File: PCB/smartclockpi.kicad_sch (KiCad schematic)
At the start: 17 parts, among them J1 Raspberry_Pi_2_3, J2 DS3231 RTC module, J3 ILI9488 SPI TFT touchscreen, J4 PCM5102A DAC (with headphone 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, U1 BME280, U2 MCP3008

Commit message: finallise pcb. spent toooo much time on this...
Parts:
- removed R10, R11: 4.7kΩ, Resistor_THT:R_Axial_DIN0204_L3.6mm_D1.6mm_P5.08mm_Vertical, symbol Device:R
- removed U1: BME280, Connector_PinSocket_2.54mm:PinSocket_1x06_P2.54mm_Vertical, symbol Sensor:BME280
- added R12, R13: 4.7kΩ, Resistor_THT:R_Axial_DIN0204_L3.6mm_D1.6mm_P5.08mm_Vertical, symbol Device:R
- added U3: DHT22, Sensor:Aosong_DHT11_5.5x12.0_P2.54mm, symbol Sensor:DHT11
- J2: footprint Connector_PinSocket_2.54mm:PinSocket_1x07_P2.54mm_Vertical -> Connector_PinSocket_2.54mm:PinSocket_1x06_P2.54mm_Horizontal
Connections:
- net +3.3V: now also J2.5 (VCC), J3.1 (VCC), U3.1 (VDD); no longer J2.VCC (Pin_5), J3.VCC
- net +5V: now also J4.6 (VIN); no longer J4.VIN (Pin_6)
- net GND: now also J2.6 (GND), J3.2 (GND), J4.5 (GND), R12.2, R13.2, U3.4 (GND); no longer J2.GND (Pin_6), J3.GND, J4.GND (Pin_5)
- net at J1.12 (GPIO18/PWM0): now also J4.2 (BCK); no longer J4.BCK (Pin_2)
- net at J1.40 (GPIO21/SCLK1): now also J4.3 (DIN); no longer J4.DIN (Pin_3)
- net at J1.35 (GPIO19/MISO1): now also J4.4 (LCK); no longer J4.LCK (Pin_4)
- net at J1.24 (~{CE0}/GPIO8): now also J3.3 (CS); no longer J3.CS
- net at J1.18 (GPIO24): now also J3.5 (DC/RS); no longer J3.DC/RS
- net at J1.33 (PWM1/GPIO13): now also J3.8 (LED); no longer J3.LED
- net at J1.21 (MISO0/GPIO9), U2.12 (Dout): now also J3.9 (MISO); no longer J3.MISO
- net at J1.19 (MOSI0/GPIO10), U2.11 (Din): now also J3.6 (MOSI); no longer J3.MOSI
- net at J1.22 (GPIO25): now also J3.4 (RESET); no longer J3.RESET
- net at J1.23 (SCLK0/GPIO11), U2.13 (CLK): now also J3.7 (SCK); no longer J3.SCK
- net at J1.31 (GCLK2/GPIO6): now also J3.10 (T_CLK); no longer J3.T_CLK
- net at J1.29 (GCLK1/GPIO5): now also J3.11 (T_CS); no longer J3.T_CS
- net at J1.32 (PWM0/GPIO12): now also J3.12 (T_DIN); no longer J3.T_DIN
- net at J1.16 (GPIO23): now also J3.13 (T_DO); no longer J3.T_DO
- net at J1.36 (GPIO16): now also J3.14 (T_IRQ); no longer J3.T_IRQ
- net at J1.3 (SDA/GPIO2): now also J2.4 (SDA); no longer J2.SDA (Pin_4)
- net at J1.5 (SCL/GPIO3): now also J2.3 (SCL); no longer J2.SCL (Pin_3)
- net at J1.26 (~{CE1}/GPIO7): now also U3.2 (DATA)
- new net: J2.2 (SQW), R13.1
- new net: J2.1 (32K), R12.1
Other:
- moved on the sheet: J3

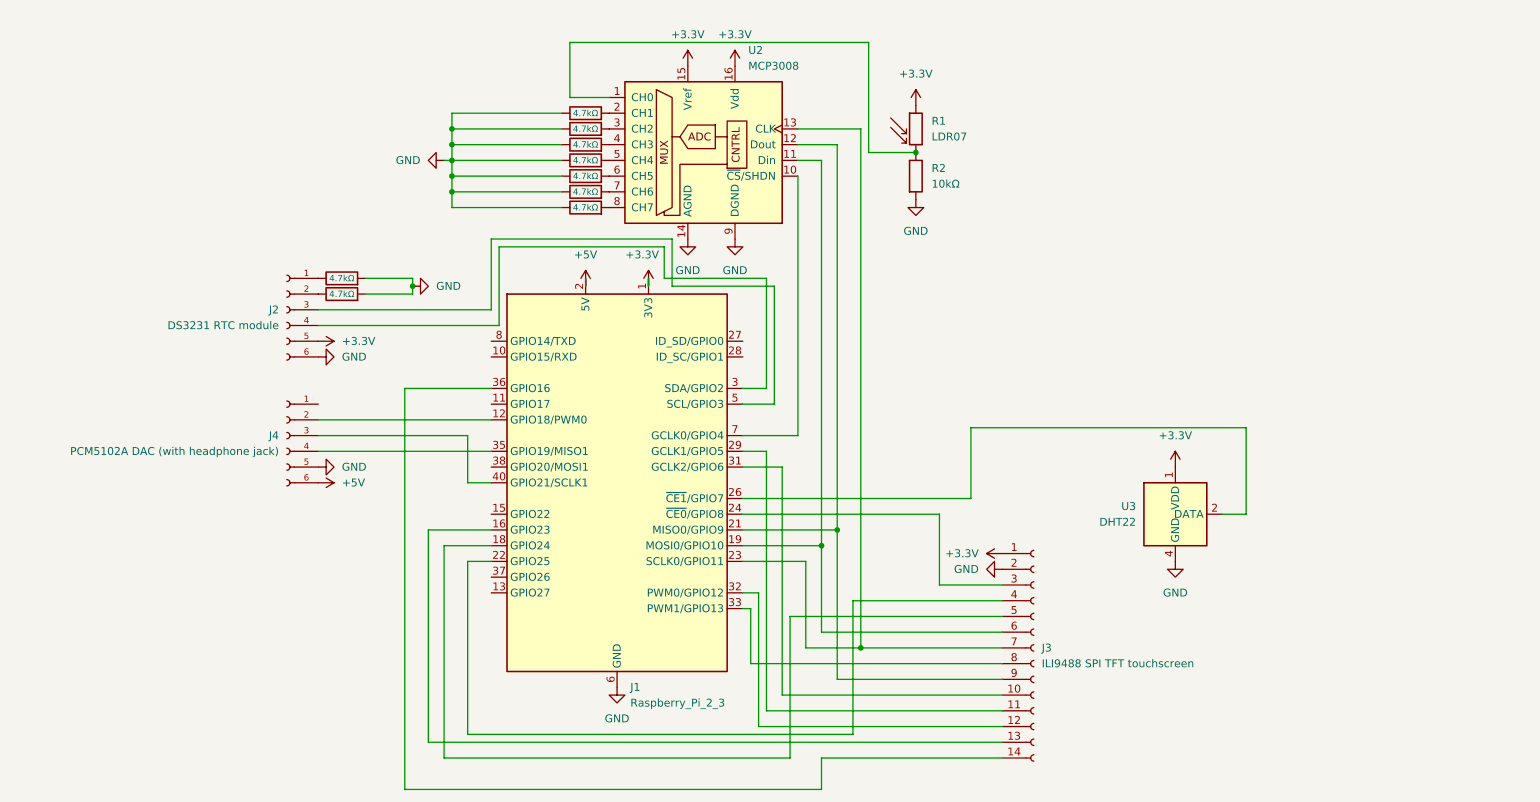
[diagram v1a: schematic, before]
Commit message: add in usb ports
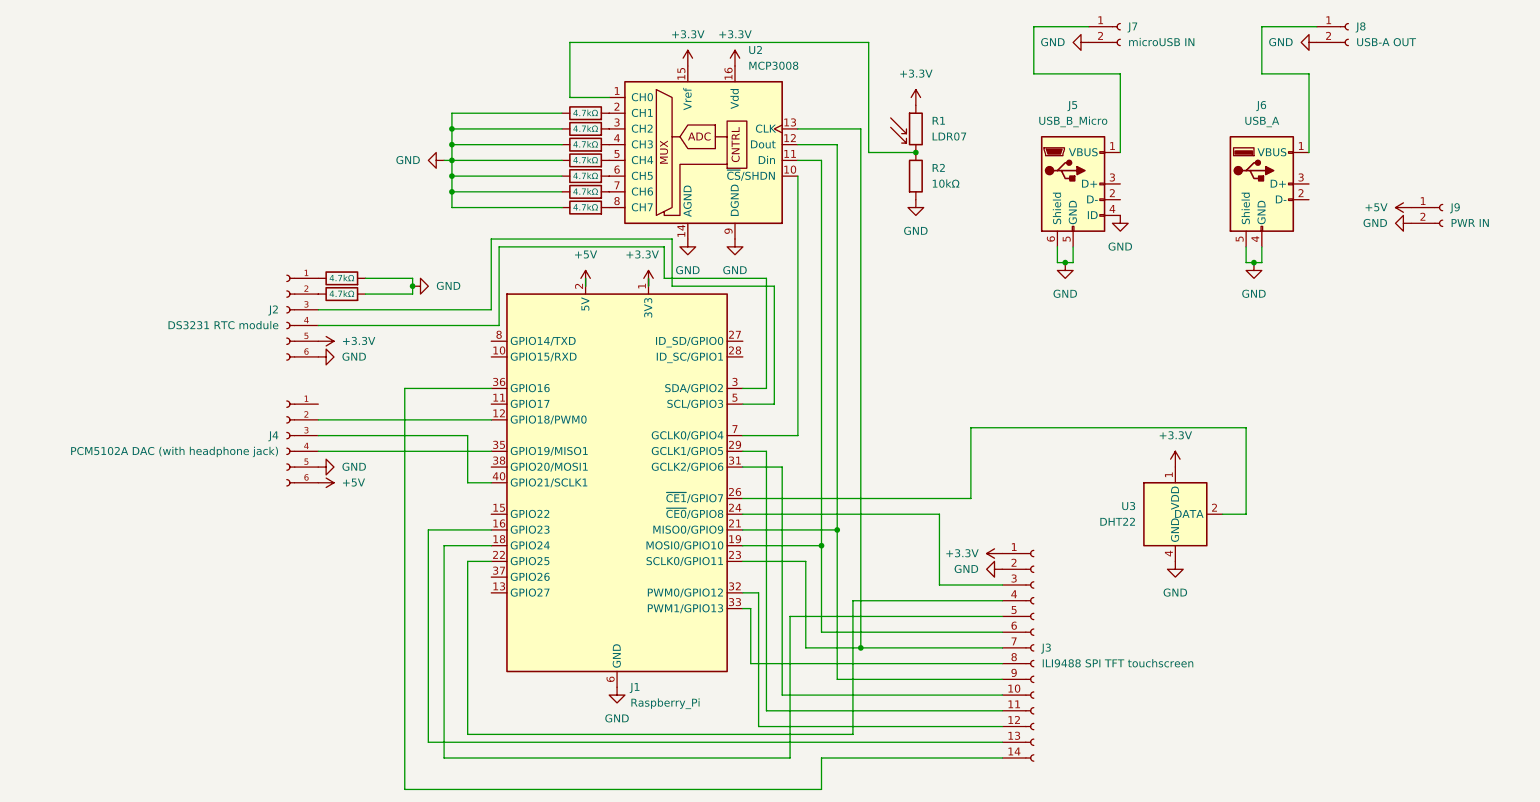
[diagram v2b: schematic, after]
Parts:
- added J5: USB_B_Micro, Connector_USB:USB_Micro-B_Amphenol_10118193-0001LF_Horizontal, symbol Connector:USB_B_Micro
- added J6: USB_A, Connector_USB:USB_A_Receptacle_GCT_USB1046, symbol Connector:USB_A
- added J7: microUSB IN, Connector_PinSocket_2.54mm:PinSocket_1x02_P2.54mm_Vertical, symbol Connector:Conn_01x02_Socket
- added J8: USB-A OUT, Connector_PinSocket_2.54mm:PinSocket_1x02_P2.54mm_Vertical, symbol Connector:Conn_01x02_Socket
- added J9: PWR IN, Connector_PinSocket_2.54mm:PinSocket_1x02_P2.54mm_Vertical, symbol Connector:Conn_01x02_Socket
- J1: value Raspberry_Pi_2_3 -> Raspberry_Pi
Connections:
- net +5V: now also J9.1 (Pin_1)
- net GND: now also J5.4 (ID), J5.5 (GND), J5.6 (Shield), J6.4 (GND), J6.5 (Shield), J7.2 (Pin_2), J8.2 (Pin_2), J9.2 (Pin_2)
- new net: J6.1 (VBUS), J8.1 (Pin_1)
- new net: J5.1 (VBUS), J7.1 (Pin_1)

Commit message: update PCB
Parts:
- added D1: 1N4001, Diode_THT:D_DO-41_SOD81_P10.16mm_Horizontal, symbol Diode:1N4001
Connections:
- net +5V: now also D1.1 (K); no longer J9.1 (Pin_1)
- new net: D1.2 (A), J9.1 (Pin_1)
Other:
- moved on the sheet: J9

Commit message: update pcb and stuff
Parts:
- removed J4: PCM5102A DAC (with headphone jack), Connector_PinSocket_2.54mm:PinSocket_1x06_P2.54mm_Vertical, symbol Connector:Conn_01x06_Socket
- J1: footprint Connector_PinSocket_2.54mm:PinSocket_2x20_P2.54mm_Vertical -> Connector_PinHeader_2.54mm:PinHeader_2x20_P2.54mm_Vertical
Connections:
- net at J1.40 (GPIO21/SCLK1): now also J3.10 (T_CLK)
- net at J1.35 (GPIO19/MISO1): now also J3.12 (T_DIN)
- net at J1.31 (GCLK2/GPIO6): no longer J3.10 (T_CLK)
- net at J3.11 (T_CS): now also J1.38 (GPIO20/MOSI1); no longer J1.29 (GCLK1/GPIO5)
- net at J1.32 (PWM0/GPIO12): now also J3.14 (T_IRQ); no longer J3.12 (T_DIN)
- net at J3.13 (T_DO): now also J1.11 (GPIO17); no longer J1.16 (GPIO23)
- net at J1.36 (GPIO16): no longer J3.14 (T_IRQ)
- net at J1.26 (~{CE1}/GPIO7): now also U2.10 (~{CS}/SHDN); no longer U3.2 (DATA)
- net at J1.7 (GCLK0/GPIO4): now also U3.2 (DATA); no longer U2.10 (~{CS}/SHDN)
